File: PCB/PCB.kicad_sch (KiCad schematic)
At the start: 16 parts, among them J1 Barrel_Jack_Switch, U1 TSV782, U2 TLV3542, U3 LDK320

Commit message: schematic progress
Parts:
- added C10, C11, C12, C13: 100n, symbol Device:C
- added R10, R11, R7, R8, R9: 10k, symbol Device:R
- added R3: 10M, symbol Device:R
- added R4: 100k, symbol Device:R
- added R5: 1k, symbol Device:R
- added R6: 100R, symbol Device:R
- added SW1, SW2: SW_Push, symbol Switch:SW_Push
- added U4: 74HC193, w-ic:SOIC-16 3.9x9.9mm P1.27mm, symbol 74xx:74HC193
- added U5: 74HC139, w-ic:SOIC-16 3.9x9.9mm P1.27mm, symbol w-digital-ic:74HC139
- added U6: 74HC14, symbol 74xx:74HC14
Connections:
- net +5V: now also C10.1, C11.1, R10.1, R7.1, R8.1, U4.16 (VCC), U5.16 (VCC)
- net GND: now also C10.2, C11.2, C12.2, C13.2, SW1.1, SW2.1, U4.1 (B), U4.10 (C), U4.14 (CLR), U4.15 (A), U4.8 (GND), U4.9 (D), U5.1 (~{E1}), U5.13 (2A1), U5.14 (2A0), U5.15 (~{E2}), U5.8 (GND)
- new net: C13.1, R11.2, U6.13
- new net: R8.2, R9.1, SW1.2
- new net: C12.1, R9.2, U6.11
- new net: U5.4 (~{1Y0}), U6.1
- new net: R10.2, R11.1, SW2.2
- new net: U5.6 (~{1Y2}), U6.5
- new net: U5.5 (~{1Y1}), U6.3
- new net: R7.2, U4.11 (~{LOAD})
- new net: U5.7 (~{1Y3}), U6.9
- new net CT_DOWN: U4.4 (DOWN)
- new net CT_LSB: U4.3 (QA), U5.2 (1A0)
- new net CT_MSB: U4.2 (QB), U5.3 (1A1)
- new net CT_UP: U4.5 (UP)
- new net R1: U6.8
- new net R2: U6.6
- new net R3: U6.4
- new net R4: U6.2
- no-connect marks 1 -> 9
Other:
- note added: "přičítání zmenšuje range"
- note added: "range+"
- note added: "range-"
- moved on the sheet: U1A, U2B

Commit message: range switching
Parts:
- removed C10, C11, C12, C13: 100n, symbol Device:C
- removed R10, R11, R7, R8, R9: 10k, symbol Device:R
- removed R4: 100k, symbol Device:R
- removed R5: 1k, symbol Device:R
- removed R6: 100R, symbol Device:R
- removed U4: 74HC193, w-ic:SOIC-16 3.9x9.9mm P1.27mm, symbol 74xx:74HC193
- removed U5: 74HC139, w-ic:SOIC-16 3.9x9.9mm P1.27mm, symbol w-digital-ic:74HC139
- removed U6: 74HC14, symbol 74xx:74HC14
- added D101, D102, D103, D104: SS24, Diode_SMD:D_SMA, symbol Diode:SS24
- added J101: Current_input, symbol Connector:Screw_Terminal_01x02
- added J102: Conn_Coaxial, symbol Connector:Conn_Coaxial
- added Q101, Q102, Q103, Q104: BC817, w-ic:SOT-23, symbol Transistor_BJT:BC817
- added R101, R102, R104, R105: 4k7, symbol Device:R
- added R103, R110, R111, R112, R115: 100k, symbol Device:R
- added R106: 100R, symbol Device:R
- added R107: 1k, symbol Device:R
- added R108, R109: R, symbol Device:R
- added R113, R114: 51k, symbol Device:R
- added U101: 74HC00, symbol 74xx:74HC00
- added U102, U103, U104, U105: OJ-SH-105HM, w-relay:TE Connectivity Relay, symbol w-switch:OJ-SH-105HM
- added U106: TLV3542, w-ic:SOIC-8, symbol w-analog-ic:TLV3542
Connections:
- net +5V: now also D101.1 (K), D102.1 (K), D103.1 (K), D104.1 (K), R108.1, U101.10, U101.12, U102.2, U103.2, U104.2, U105.2
- net GND: now also Q101.2 (E), Q102.2 (E), Q103.2 (E), Q104.2 (E), R109.2, R112.1, R115.1
- net GNDA: now also U1.3 (+), J101.2 (Pin_2), J102.2 (Ext), U106.5 (+)
- net range_selector/RNG+: now reaches SW1.2
- net range_selector/RNG-: now reaches SW2.2
- net at R3.1: now also U102.3
- net at R3.2: now also U1.1, U2.5 (+), R103.2, R106.2, R107.2
- net at U2.6 (-): now also U2.7, R110.1, R113.1
- net at U1.5 (+): now also R108.2, R109.1
- net CURR_OUT: now reaches U1.2 (-)
- net CURR_OUT: now also J101.1 (Pin_1), U102.4, U103.4, U104.4, U105.4
- new net: Q104.1 (B), R105.2
- new net: R106.1, U104.3
- new net: R112.2, R113.2, U101.9
- new net: D101.2 (A), Q101.3 (C), U102.2
- new net: D103.2 (A), Q103.3 (C), U104.2
- new net: Q101.1 (B), R101.2
- new net: D104.2 (A), Q104.3 (C), U105.2
- new net: Q103.1 (B), R104.2
- new net: D102.2 (A), Q102.3 (C), U103.2
- new net: U101.11, U101.8
- new net: R114.2, R115.2, U101.13
- new net: Q102.1 (B), R102.2
- new net: R111.2, R114.1, U106.7
- new net: R103.1, U103.3
- new net: R110.2, R111.1, U106.6 (-)
- new net: R107.1, U105.3
- new net range_selector/R1: R104.1
- new net range_selector/R2: R105.1
- new net range_selector/R3: R102.1
- new net range_selector/R4: R101.1
- no-connect marks 9 -> 1
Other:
- added sheet range_selector (range_selector.kicad_sch)
- note added: "+"
- note added: "-"
- note added: "100nA/1V"
- note added: "10mA/1V"
- note added: "10uA/1V"
- note added: "1mA/1V"
- note added: "ISNS"
- note added: "Range+"
- note added: "Range-"
- note removed: "přičítání zmenšuje range"
- note removed: "range+"
- note removed: "range-"
- moved on the sheet: C1, C2, C3, C4, C5, C6, C7, C8, C9, FB1, J1, R1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

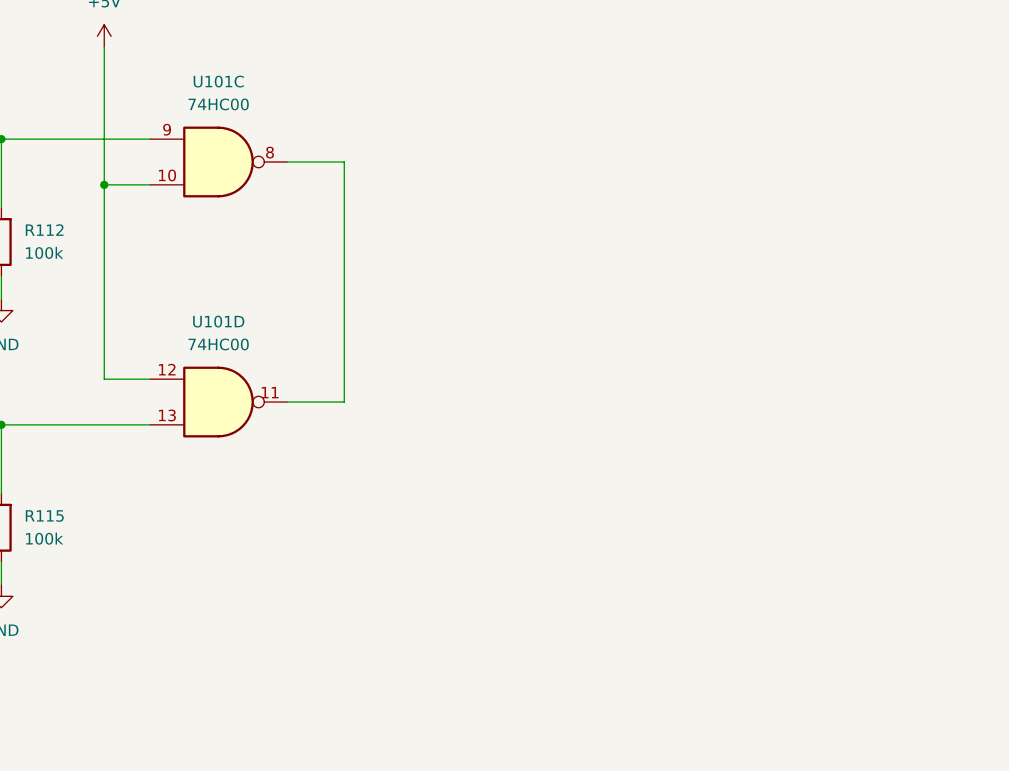
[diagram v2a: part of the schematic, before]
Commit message: astable op amp
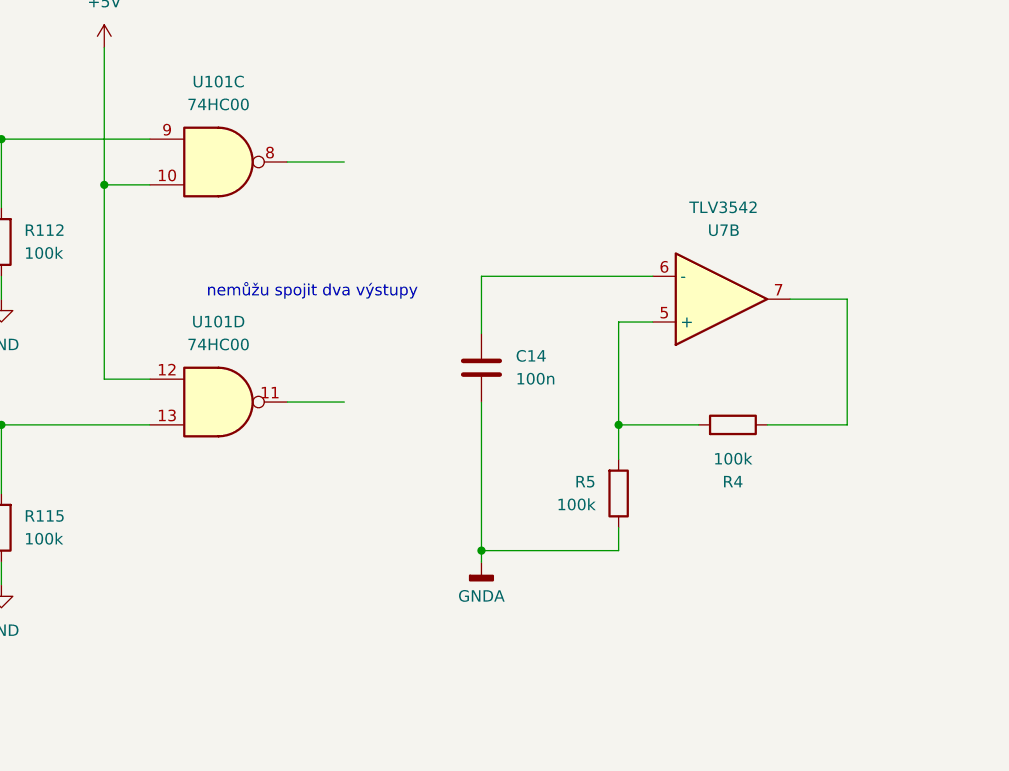
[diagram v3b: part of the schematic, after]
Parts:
- added C14: 100n, symbol Device:C
- added R4, R5: 100k, symbol Device:R
- added U7: TLV3542, w-ic:SOIC-8, symbol w-analog-ic:TLV3542
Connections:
- net GNDA: now also C14.2, R5.1
- net at U101.11: no longer U101.8
- new net: R4.2, R5.2, U7.5 (+)
- new net: C14.1, U7.6 (-)
- new net: R4.1, U7.7
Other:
- note added: "nemůžu spojit dva výstupy"

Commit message: schematic roughly done
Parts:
- removed C1, C2, C7, C8: 1u, symbol Device:C
- removed C14, C5, C6: 100n, symbol Device:C
- removed C3, C4: 100u, symbol Device:C_Polarized
- removed FB1: FerriteBead, symbol Device:FerriteBead
- removed J1: Barrel_Jack_Switch, symbol Connector:Barrel_Jack_Switch
- removed R1, R110, R111, R112, R115, R2, R4, R5: 100k, symbol Device:R
- removed R108, R109: R, symbol Device:R
- removed R113, R114: 51k, symbol Device:R
- removed unit 3 of U1
- removed unit 2 of U1
- removed U101: 74HC00, symbol 74xx:74HC00
- removed U106, U7: TLV3542, w-ic:SOIC-8, symbol w-analog-ic:TLV3542
- removed unit 1 of U2
- removed unit 3 of U2
- removed U3: LDK320, w-ic:SOT-89-3, symbol w-regulator:LDK320
- added C101: 2u2, symbol Device:C
- added J103: Conn_01x02_Socket, symbol Connector:Conn_01x02_Socket
- added R117: 100k, symbol Device:R
- added R118: 51R, symbol Device:R
- added U107, U401: TSV782, w-ic:SOIC-8, symbol w-analog-ic:TSV782
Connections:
- net +5V: no longer C9.1
- net GND: now also C101.2, J103.2 (Pin_2), U107.4 (V-)
- net at R103.2, R106.2, R107.2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: now also R118.1
- net overrange_detecor/IN: now reaches U2.6 (-), U2.7
- net overrange_detecor/IN: now also R117.1
- net at J102.1 (In): now also R118.2
- new net: C101.1, J103.1 (Pin_1), R117.2
- new net +5VA: C9.1, U107.8 (V+)
- no-connect marks 1 -> 0
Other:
- added sheet overrange_detecor (overrange_detecor.kicad_sch)
- added sheet power_supply (power_supply.kicad_sch)
- note added: "Average out"
- note added: "BNC out"
- note added: "f_{0} = 0,7 Hz"
- note removed: "nemůžu spojit dva výstupy"
- moved on the sheet: C9, D101, D102, D103, D104, J101, J102, Q101, Q102, Q103, Q104, R101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

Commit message: footprints
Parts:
- removed U1, U107, U401: TSV782, w-ic:SOIC-8, symbol w-analog-ic:TSV782
- removed U2: TLV3542, w-ic:SOIC-8, symbol w-analog-ic:TLV3542
- added U101: TSV782, w-ic:SOIC-8, symbol w-analog-ic:TSV782
- C101: renamed from C9; footprint (none) -> Capacitor_SMD:C_0603_1608Metric
- C102: renamed from C101; footprint (none) -> Capacitor_SMD:C_0603_1608Metric
- R101: renamed from R104; footprint (none) -> Resistor_SMD:R_0603_1608Metric
- R102: renamed from R105; footprint (none) -> Resistor_SMD:R_0603_1608Metric
- R103: renamed from R102; footprint (none) -> Resistor_SMD:R_0603_1608Metric
- R104: renamed from R101; footprint (none) -> Resistor_SMD:R_0603_1608Metric
- R109: renamed from R118; footprint (none) -> Resistor_SMD:R_0603_1608Metric
- R110: renamed from R117; footprint (none) -> Resistor_SMD:R_0603_1608Metric
- renumbered D103 to D101, D104 to D102, D102 to D103, D101 to D104, J103 to J102, J102 to J103, Q103 to Q101, Q104 to Q102, Q102 to Q103, Q101 to Q104, R106 to R105, R107 to R106, R103 to R107, R3 to R108, SW1 to SW101, SW2 to SW102, U104 to U102, U105 to U103, U103 to U104, U102 to U105
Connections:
- net +5VA: now also U101.8 (V+)
- net CURR_OUT: now also U101.2 (-)
- net GND: now also U101.4 (V-)
- net GNDA: now also U101.3 (+)
- net overrange_detecor/IN: now also U101.6 (-), U101.7
- net at R105.2, R106.2, R107.2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: now also U101.1, U101.5 (+)

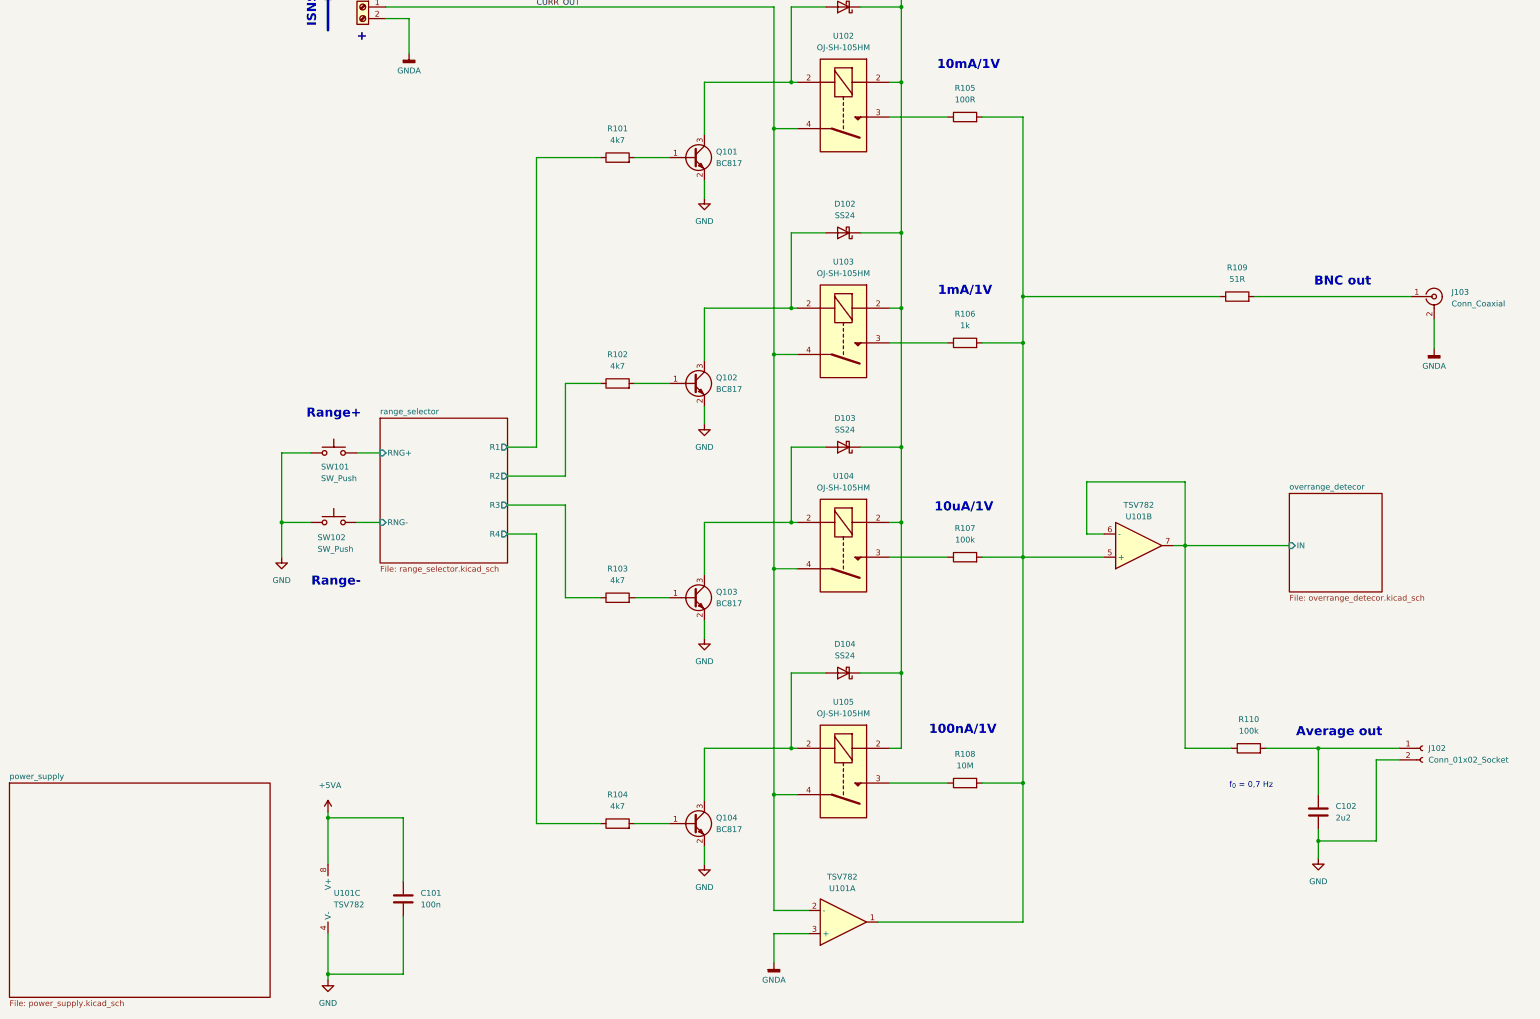
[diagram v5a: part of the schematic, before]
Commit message: footprints and overrange detector timing
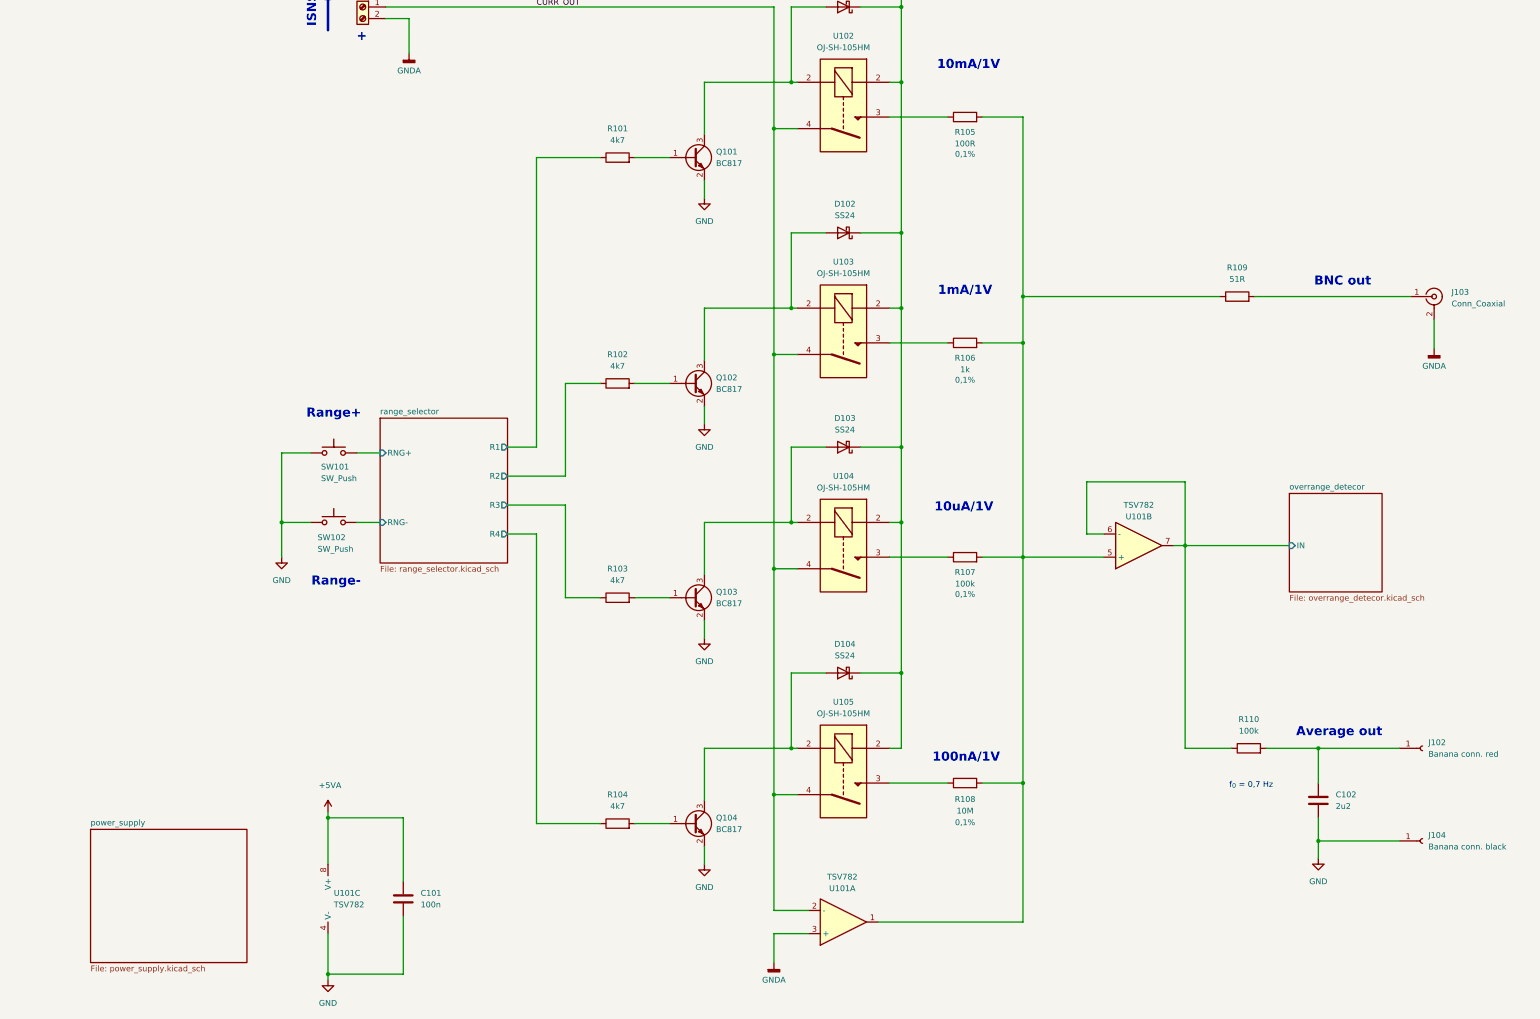
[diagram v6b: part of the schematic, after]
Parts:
- removed J102: Conn_01x02_Socket, symbol Connector:Conn_01x02_Socket
- added J102: Banana conn. red, symbol Connector:Conn_01x01_Socket
- added J104: Banana conn. black, symbol Connector:Conn_01x01_Socket
- J101: footprint (none) -> TerminalBlock_Phoenix:TerminalBlock_Phoenix_MPT-0,5-2-2.54_1x02_P2.54mm_Horizontal
- R105, R106, R107: footprint (none) -> Resistor_SMD:R_0603_1608Metric; Tol (none) -> 0,1%
- R108: footprint (none) -> Resistor_SMD:R_1206_3216Metric; Mouser (none) -> MCA1206MD1005BP500; Tol (none) -> 0,1%
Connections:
- net GND: now also J104.1 (Pin_1)
- net at C102.1, R110.2: now also J102.1 (Pin_1)
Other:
- moved on the sheet: C102

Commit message: changes
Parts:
- D101, D102, D103, D104: footprint Diode_SMD:D_SMA -> w-diode:SOD-123LF
- J102: footprint (none) -> w-connector:J.40024.2
- J103: renamed from J104; footprint (none) -> w-connector:J.40024.2
- J104: renamed from J103; footprint (none) -> w-connector:GOLDEN LOCH 900D-6452R2
- SW101, SW102: footprint (none) -> Connector_PinHeader_2.54mm:PinHeader_1x02_P2.54mm_Vertical; Store (none) -> https://cz.mouser.com/ProductDetail/Adam-Tech/SW-PB1-1DZ-A-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
- renumbered C102 to C101, C101 to C102
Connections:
- net GND: no longer C101.2, J103.1 (Pin_1)
- net GNDA: now also C101.2, J103.1 (Pin_1)
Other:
- note added: "Guard ring"
- moved on the sheet: C101, C102, J101, J102, J103, Q101, Q102, Q103, Q104, R101, R102, R103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

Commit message: start of layout
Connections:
- net +5V: now also U102.1, U103.1, U104.1, U105.1; no longer U102.2, U103.2, U104.2, U105.2
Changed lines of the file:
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@@
 	)
 	(symbol
-		(lib_name "OJ-SH-105HM_3")
 		(lib_id "w-switch:OJ-SH-105HM")
 		(at 217.17 63.5 270)
@@
 		(pin "2"
 		)
-		(pin "2"
+		(pin "1"
 		)
 		(pin "3"
@@
 		(pin "2"
 		)
-		(pin "2"
+		(pin "1"
 		)
 		(pin "3"
@@
 	)
 	(symbol
-		(lib_name "OJ-SH-105HM_1")
 		(lib_id "w-switch:OJ-SH-105HM")
 		(at 217.17 160.02 270)
@@
 		(pin "2"
 		)
-		(pin "2"
+		(pin "1"
 		)
 		(pin "3"
@@
 	)
 	(symbol
-		(lib_name "OJ-SH-105HM_2")
 		(lib_id "w-switch:OJ-SH-105HM")
 		(at 217.17 113.03 270)
@@
 		(pin "2"
 		)
-		(pin "2"
+		(pin "1"
 		)
 		(pin "3"
